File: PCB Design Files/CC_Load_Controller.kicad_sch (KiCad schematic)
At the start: 40 parts, among them M201 Fan, Q201 IRF3205, Q202 IRF3205, Q203 IRF3205, Q204 IRF3205, U201 TLV9162

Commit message: Finished board layout
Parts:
- added NT203, NT204, NT205, NT206: (no value), symbol Device:NetTie_2
- HS201: footprint (none) -> irex_Heatsink:Heatsink_HeatsinkUSA_3.00x1.65in_2xDrill5.25mm_TO-220-Mount
- M201: value Fan -> (none); footprint Connector_JST:JST_XH_B2B-XH-AM_1x02_P2.50mm_Vertical -> (none)
- Q201, Q202, Q203, Q204: footprint Resistor_SMD:R_0603_1608Metric -> Package_TO_SOT_THT:TO-220-3_Vertical
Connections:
- net Vsense_A: now also NT205.2; no longer R208.1
- net Vsense_B: now also NT206.2; no longer R209.1
- net Vsense_FET_A: now also NT203.2; no longer R206.1
- net Vsense_FET_B: now also NT204.2; no longer R207.1
- new net Vsense_A_NT: NT205.1, R208.1
- new net Vsense_B_NT: NT206.1, R209.1
- new net Vsense_FET_A_NT: NT203.1, R206.1
- new net Vsense_FET_B_NT: NT204.1, R207.1
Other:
- moved on the sheet: R206, R207, R208, R209

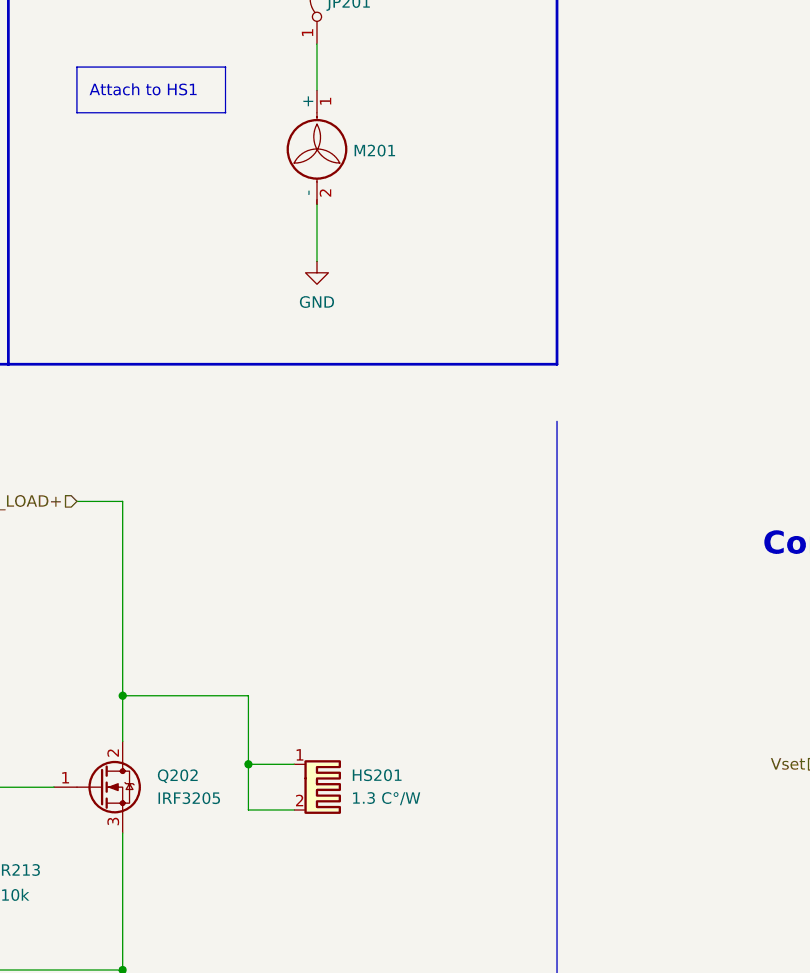
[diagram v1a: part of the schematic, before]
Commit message: Added fan shroud 3D model and heatsink drawing
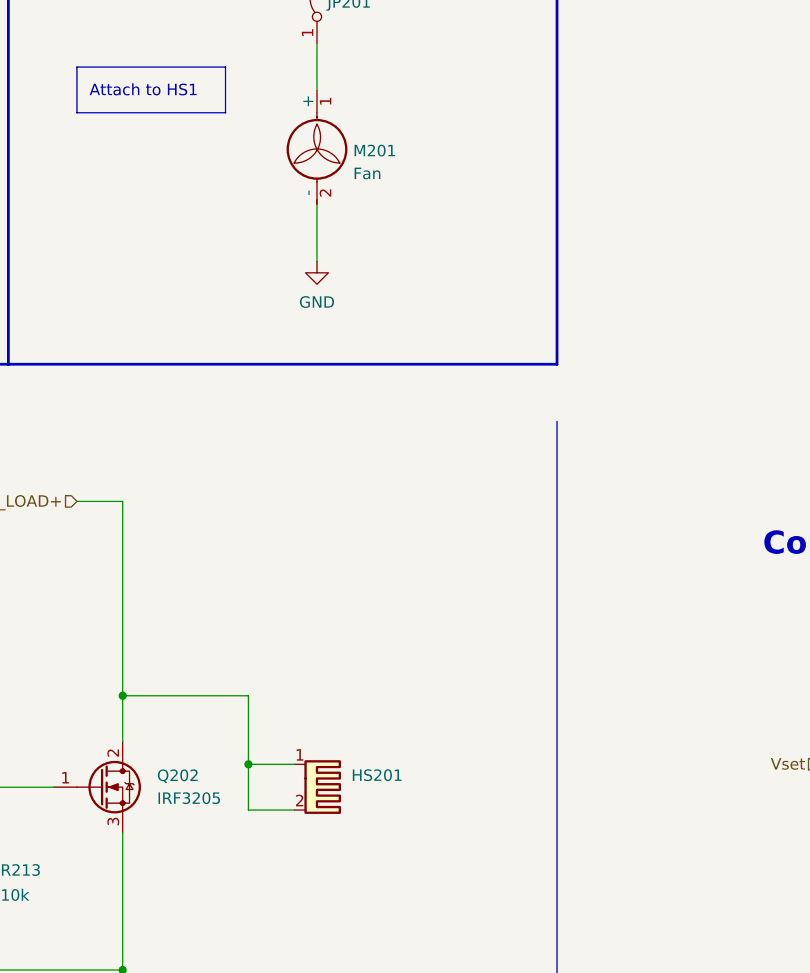
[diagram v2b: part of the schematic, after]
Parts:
- HS201: value 1.3 C°/W -> (none); footprint irex_Heatsink:Heatsink_HeatsinkUSA_3.00x1.65in_2xDrill5.25mm_TO-220-Mount -> (none); MPN (none) -> 2.000-S
- M201: value (none) -> Fan; footprint (none) -> Connector_JST:JST_XH_B2B-XH-A_1x02_P2.50mm_Vertical
- NT203, NT204, NT205, NT206: value (none) -> NetTie_2; footprint (none) -> irex_NetTie:NetTie-2_SMD_Pad12.0mils
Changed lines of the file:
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@@
       (effects (font (size 1.27 1.27)) (justify left))
     )
-    (property "Value" "" (id 1) (at 195.7832 61.3922 0)
-      (effects (font (size 1.27 1.27)) (justify left))
-    )
-    (property "Footprint" "" (id 2) (at 191.77 59.436 0)
+    (property "Value" "Fan" (id 1) (at 195.7832 61.3922 0)
+      (effects (font (size 1.27 1.27)) (justify left))
+    )
+    (property "Footprint" "Connector_JST:JST_XH_B2B-XH-A_1x02_P2.50mm_Vertical" (id 2) (at 191.77 59.436 0)
       (effects (font (size 1.27 1.27)) hide)
     )
@@
       (effects (font (size 1.27 1.27)) (justify left))
     )
-    (property "Value" "1.3 C°/W" (id 1) (at 195.58 130.7972 90)
-      (effects (font (size 1.27 1.27)) (justify left))
-    )
-    (property "Footprint" "irex_Heatsink:Heatsink_HeatsinkUSA_3.00x1.65in_2xDrill5.25mm_TO-220-Mount" (id 2) (at 190.5 129.8448 0)
+    (property "Value" "" (id 1) (at 195.58 130.7972 90)
+      (effects (font (size 1.27 1.27)) (justify left))
+    )
+    (property "Footprint" "" (id 2) (at 190.5 129.8448 0)
       (effects (font (size 1.27 1.27)) hide)
     )
     (property "Datasheet" "~" (id 3) (at 190.5 129.8448 0)
+      (effects (font (size 1.27 1.27)) hide)
+    )
+    (property "MPN" "2.000-S" (id 4) (at 191.77 129.54 0)
       (effects (font (size 1.27 1.27)) hide)
     )
@@
     (in_bom yes) (on_board yes)
     (property "Reference" "NT205" (id 0) (at 133.35 60.96 0))
-    (property "Value" "" (id 1) (at 133.35 61.0671 0)
-      (effects (font (size 1.27 1.27)) hide)
-    )
-    (property "Footprint" "" (id 2) (at 133.35 62.23 0)
+    (property "Value" "NetTie_2" (id 1) (at 133.35 61.0671 0)
+      (effects (font (size 1.27 1.27)) hide)
+    )
+    (property "Footprint" "irex_NetTie:NetTie-2_SMD_Pad12.0mils" (id 2) (at 133.35 62.23 0)
       (effects (font (size 1.27 1.27)) hide)
     )
@@
     (in_bom yes) (on_board yes)
     (property "Reference" "NT206" (id 0) (at 133.35 73.66 0))
-    (property "Value" "" (id 1) (at 133.35 73.7671 0)
-      (effects (font (size 1.27 1.27)) hide)
-    )
-    (property "Footprint" "" (id 2) (at 133.35 74.93 0)
+    (property "Value" "NetTie_2" (id 1) (at 133.35 73.7671 0)
+      (effects (font (size 1.27 1.27)) hide)
+    )
+    (property "Footprint" "irex_NetTie:NetTie-2_SMD_Pad12.0mils" (id 2) (at 133.35 74.93 0)
       (effects (font (size 1.27 1.27)) hide)
     )
@@
     (in_bom yes) (on_board yes)
     (property "Reference" "NT204" (id 0) (at 133.35 43.18 0))
-    (property "Value" "" (id 1) (at 133.35 43.2871 0)
-      (effects (font (size 1.27 1.27)) hide)
-    )
-    (property "Footprint" "" (id 2) (at 133.35 44.45 0)
+    (property "Value" "NetTie_2" (id 1) (at 133.35 43.2871 0)
+      (effects (font (size 1.27 1.27)) hide)
+    )
+    (property "Footprint" "irex_NetTie:NetTie-2_SMD_Pad12.0mils" (id 2) (at 133.35 44.45 0)
       (effects (font (size 1.27 1.27)) hide)
     )
@@
     (in_bom yes) (on_board yes)
     (property "Reference" "NT203" (id 0) (at 133.35 30.48 0))
-    (property "Value" "" (id 1) (at 133.35 30.5871 0)
-      (effects (font (size 1.27 1.27)) hide)
-    )
-    (property "Footprint" "" (id 2) (at 133.35 31.75 0)
-      (effects (font (size 1.27 1.27)) hide)
-    )
+    (property "Value" "NetTie_2" (id 1) (at 133.35 30.5871 0)
+      (effects (font (size 1.27 1.27)) hide)
+    )
+    (property "Footprint" "irex_NetTie:NetTie-2_SMD_Pad12.0mils" (id 2) (at 133.35 31.75 0)
+      (effects (font (size 1.27 1.27)) hide)
+    )

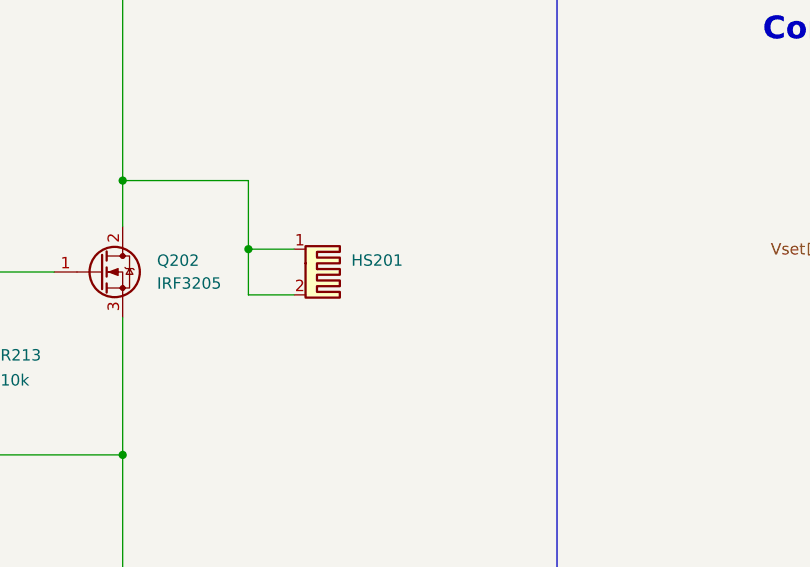
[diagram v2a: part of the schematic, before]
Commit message: Added initial prototype software
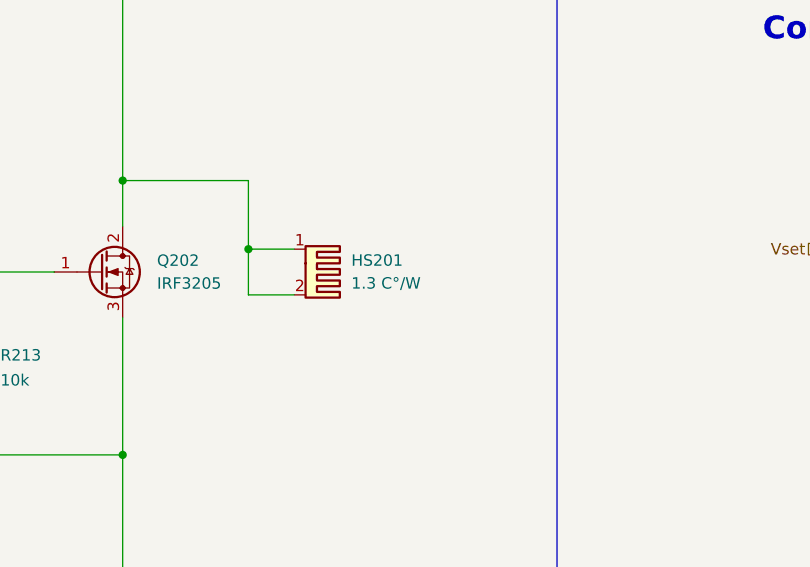
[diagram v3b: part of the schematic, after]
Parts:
- HS201: value (none) -> 1.3 C°/W; footprint (none) -> irex_Heatsink:Heatsink_HeatsinkUSA_3.00x1.65in_2xDrill5.25mm_TO-220-Mount
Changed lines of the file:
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@@
       (effects (font (size 1.27 1.27)) (justify left))
     )
-    (property "Value" "" (id 1) (at 195.58 130.7972 90)
+    (property "Value" "1.3 C°/W" (id 1) (at 195.58 130.7972 90)
       (effects (font (size 1.27 1.27)) (justify left))
     )
-    (property "Footprint" "" (id 2) (at 190.5 129.8448 0)
+    (property "Footprint" "irex_Heatsink:Heatsink_HeatsinkUSA_3.00x1.65in_2xDrill5.25mm_TO-220-Mount" (id 2) (at 190.5 129.8448 0)
       (effects (font (size 1.27 1.27)) hide)
     )
